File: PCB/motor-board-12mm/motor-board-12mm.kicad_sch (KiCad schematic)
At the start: 24 parts

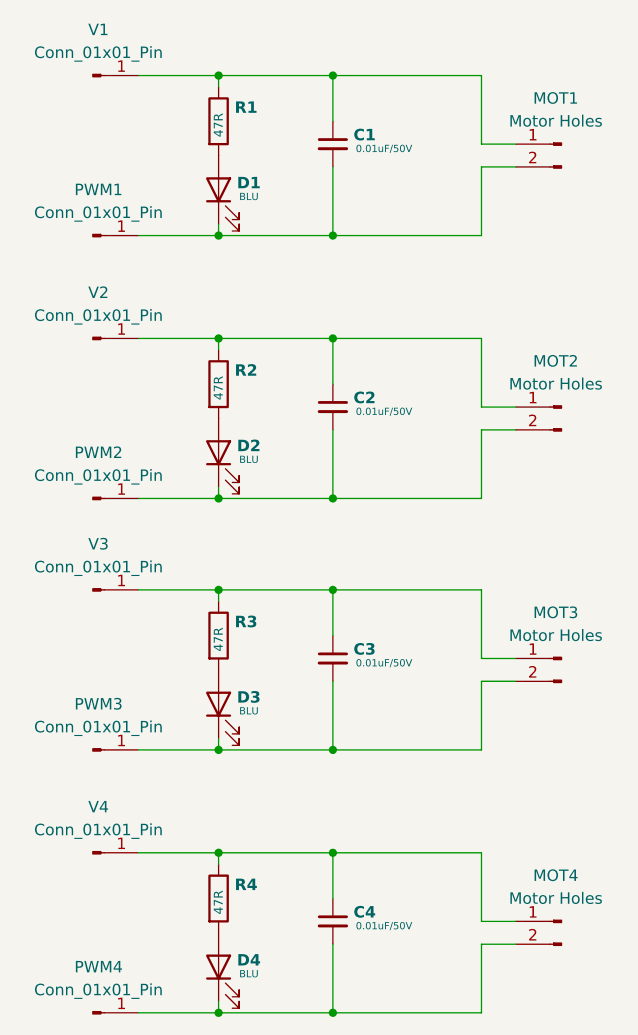
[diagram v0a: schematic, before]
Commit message: Change cap value.
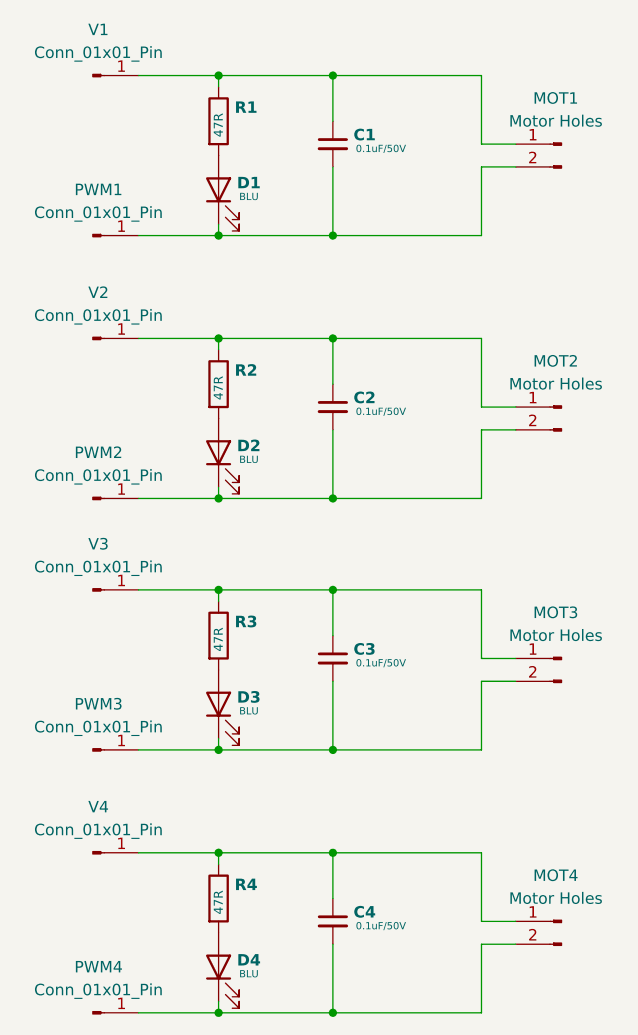
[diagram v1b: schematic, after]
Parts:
- C1, C2, C3, C4: value 0.01uF/50V -> 0.1uF/50V
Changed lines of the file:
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@@
 			)
 		)
-		(property "Value" "0.01uF/50V"
+		(property "Value" "0.1uF/50V"
 			(at 138.43 46.228 0)
 			(effects
@@
 			)
 		)
-		(property "Value" "0.01uF/50V"
+		(property "Value" "0.1uF/50V"
 			(at 138.43 132.588 0)
 			(effects
@@
 			)
 		)
-		(property "Value" "0.01uF/50V"
+		(property "Value" "0.1uF/50V"
 			(at 138.43 103.378 0)
 			(effects
@@
 			)
 		)
-		(property "Value" "0.01uF/50V"
+		(property "Value" "0.1uF/50V"
 			(at 138.43 75.438 0)
 			(effects
